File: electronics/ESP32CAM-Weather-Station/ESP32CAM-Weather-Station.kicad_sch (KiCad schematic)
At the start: 41 parts, among them IC1 BME688, IC2 SGP41-D-R4, IC3 VEML7700-TT, IC4 BQ24093DGQR, IC5 BQ29707DSET, IC6 MCP3426A0T-E_SN, IC7 TPS63070RNMR, J1 B4B-PH-SM4-TB_LF__SN_, J2 B4B-PH-SM4-TB_LF__SN_, J3 B4B-PH-SM4-TB_LF__SN_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

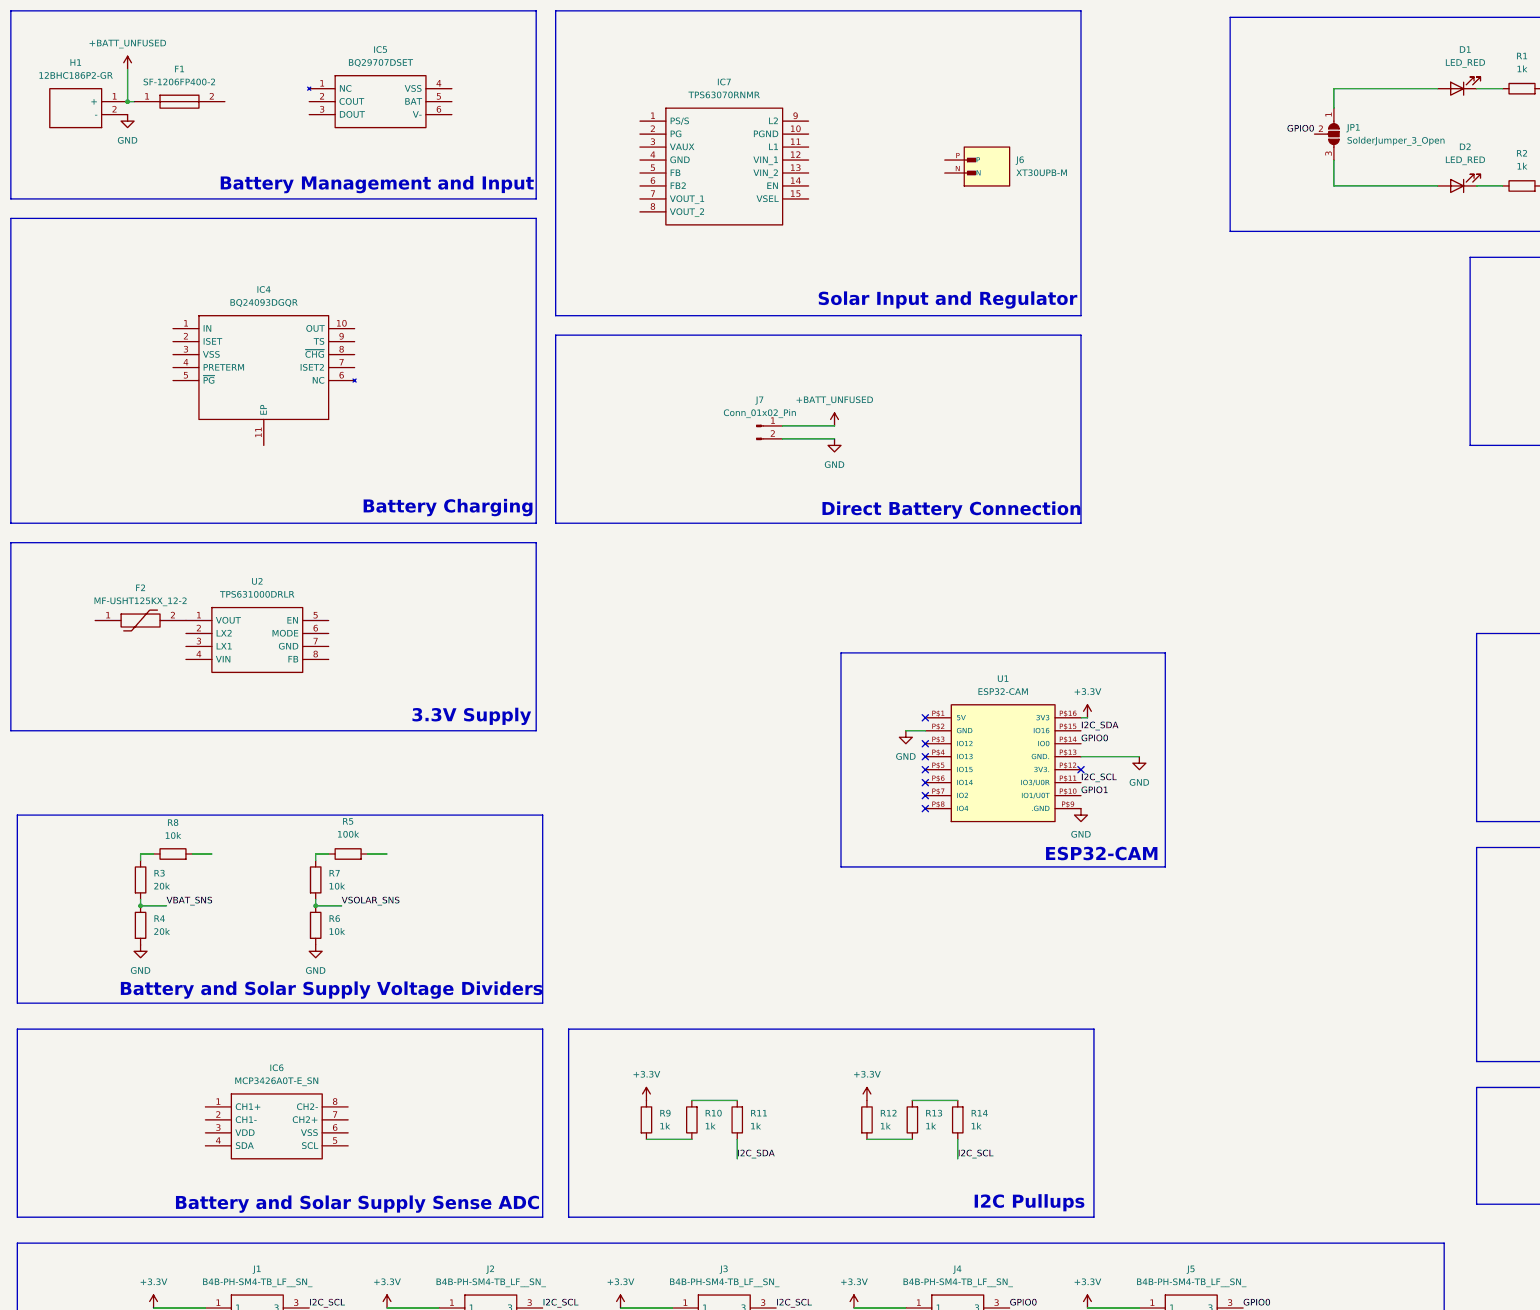
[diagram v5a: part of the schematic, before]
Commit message: [WIP] Wired battery input and protection.
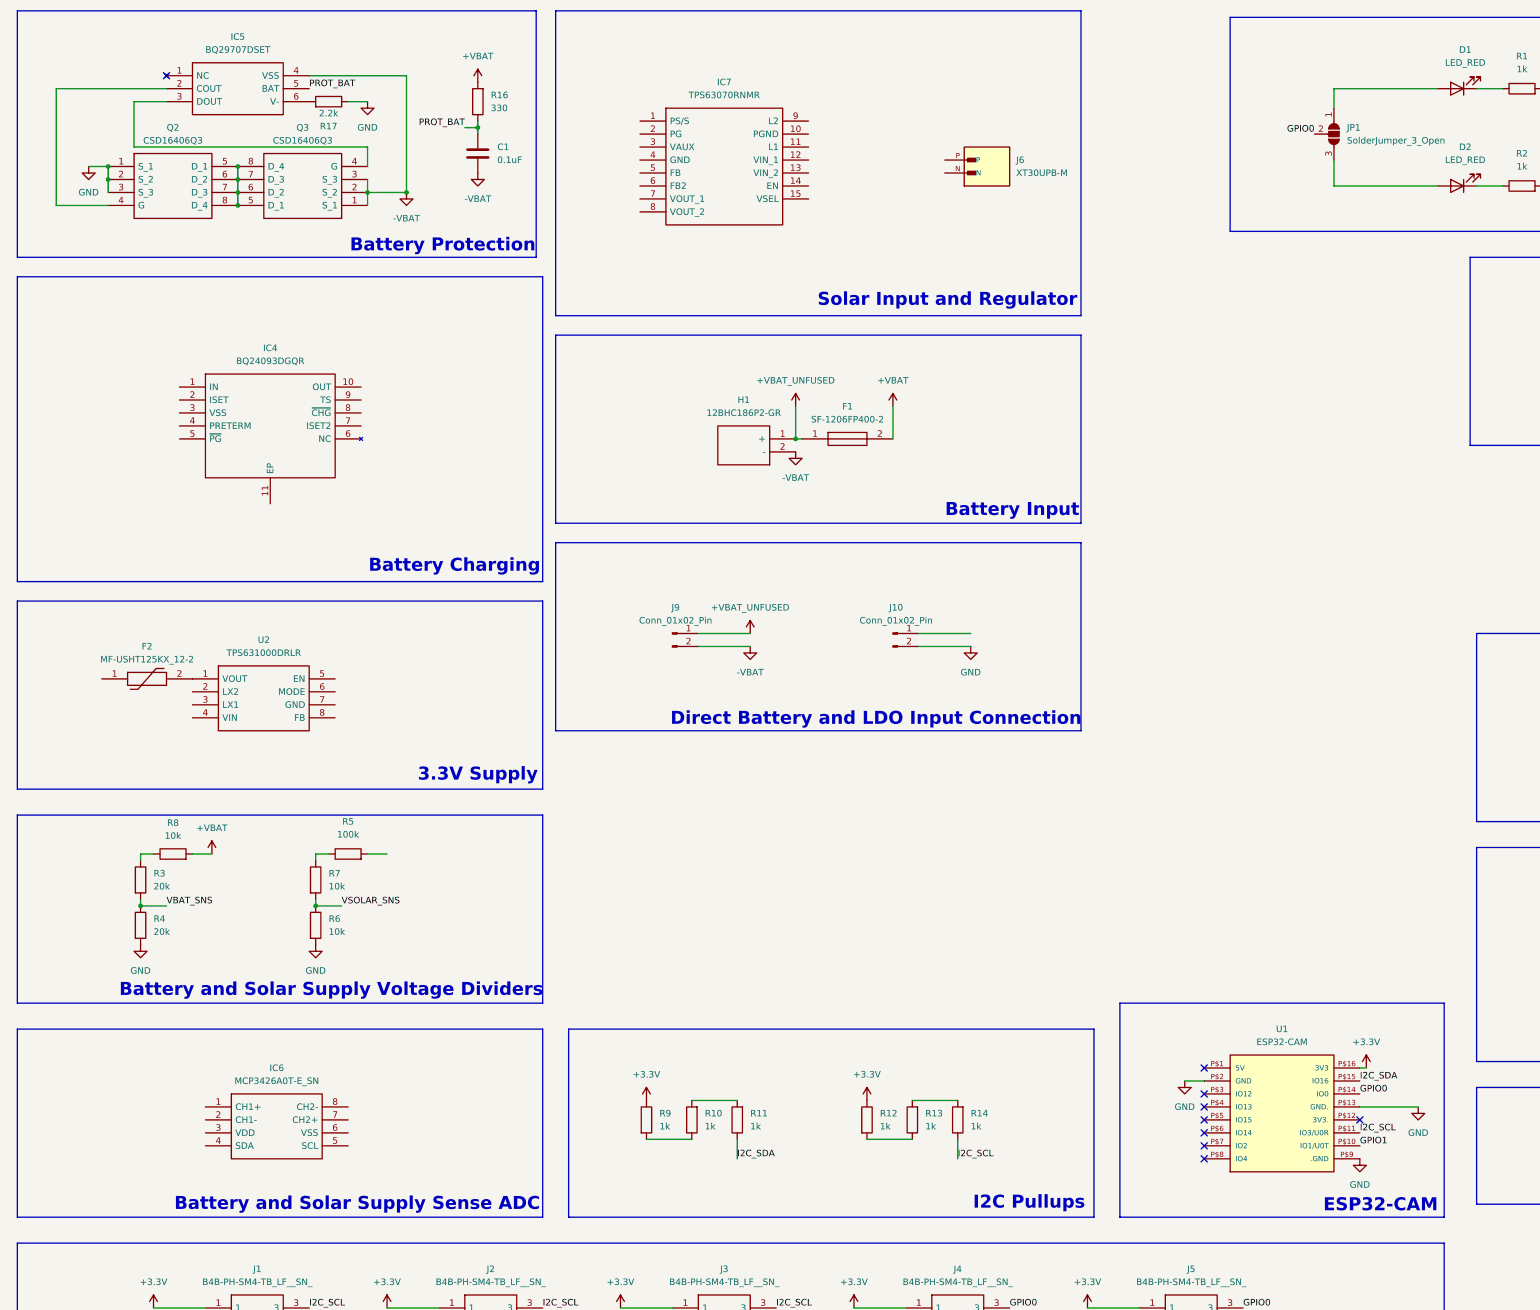
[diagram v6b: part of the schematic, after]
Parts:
- removed J7: Conn_01x02_Pin, Connector_PinHeader_2.54mm:PinHeader_1x02_P2.54mm_Vertical, symbol Connector:Conn_01x02_Pin
- added C1: 0.1uF, Capacitor_SMD:C_0805_2012Metric_Pad1.18x1.45mm_HandSolder, symbol Device:C
- added J10, J9: Conn_01x02_Pin, Connector_PinHeader_2.54mm:PinHeader_1x02_P2.54mm_Vertical, symbol Connector:Conn_01x02_Pin
- added Q2, Q3: CSD16406Q3, CSD16406Q3:DQG_VSON-CLIP, symbol CSD16406Q3:CSD16406Q3
- added R16: 330, Resistor_SMD:R_0805_2012Metric_Pad1.20x1.40mm_HandSolder, symbol Device:R
- added R17: 2.2k, Resistor_SMD:R_0805_2012Metric_Pad1.20x1.40mm_HandSolder, symbol Device:R
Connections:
- net GND: now also J10.2 (Pin_2), Q2.1 (S_1), Q2.2 (S_2), Q2.3 (S_3), R17.1; no longer H1.2 (-)
- net at IC5.2 (COUT): now also Q2.4 (G)
- net at IC5.3 (DOUT): now also Q3.4 (G)
- net -VBAT: now reaches IC5.4 (VSS)
- net -VBAT: now also H1.2 (-), C1.2, J9.2 (Pin_2), Q3.1 (S_1), Q3.2 (S_2), Q3.3 (S_3)
- net PROT_BAT: now reaches IC5.5 (BAT)
- net PROT_BAT: now also C1.1, R16.1
- net at IC5.6 (V-): now also R17.2
- net +VBAT: now reaches F1.2
- net +VBAT: now also R8.2, R16.2
- net +BATT_UNFUSED renamed +VBAT_UNFUSED
- net +VBAT_UNFUSED: now also J9.1 (Pin_1)
- new net: Q2.5 (D_1), Q2.6 (D_2), Q2.7 (D_3), Q2.8 (D_4), Q3.5 (D_1), Q3.6 (D_2), Q3.7 (D_3), Q3.8 (D_4)
- no-connect marks 10 -> 11
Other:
- note added: "Battery Input"
- note added: "Battery Protection"
- note added: "Direct Battery and LDO Input Connection"
- note removed: "Battery Management and Input"
- note removed: "Direct Battery Connection"
- moved on the sheet: F1, F2, H1, IC4, IC5, U1, U2

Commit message: [WIP] Wired battery charger for 1A charge current and 500mA preterm current.
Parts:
- removed JP2: SolderJumper_2_Open, symbol Jumper:SolderJumper_2_Open
- added C2, C3: 1uF, Capacitor_SMD:C_0805_2012Metric_Pad1.18x1.45mm_HandSolder, symbol Device:C
- added D3, D4: LED_RED, LED_SMD:LED_0805_2012Metric_Pad1.15x1.40mm_HandSolder, symbol Device:LED
- added J7: Conn_01x02_Pin, Connector_PinHeader_2.54mm:PinHeader_1x02_P2.54mm_Vertical, symbol Connector:Conn_01x02_Pin
- added JP2, JP3: SolderJumper_3_Open, symbol Jumper:SolderJumper_3_Open
- added R18, R19: 1k, Resistor_SMD:R_0805_2012Metric_Pad1.20x1.40mm_HandSolder, symbol Device:R
- added R20: 549, Resistor_SMD:R_0805_2012Metric_Pad1.20x1.40mm_HandSolder, symbol Device:R
- added R21: 10k, Resistor_SMD:R_0805_2012Metric_Pad1.20x1.40mm_HandSolder, symbol Device:R
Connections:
- net +VBAT: now also IC4.10 (OUT), C2.1, C3.1, R18.1, R19.1
- net GND: now also IC4.11 (EP), IC4.3 (VSS), IC4.7 (ISET2), C2.2, C3.2, J7.1 (Pin_1), R20.2, R21.2
- net GPIO0: now also JP1.3 (B), JP2.3 (B), JP3.3 (B); no longer JP1.2 (C)
- net GPIO1: now also JP1.1 (A), JP2.1 (A), JP3.1 (A)
- net +5V: now reaches J10.1 (Pin_1)
- net +5V: now also IC4.1 (IN)
- net at D1.2 (A): now also JP1.2 (C); no longer JP1.1 (A)
- net at R15.1: now also JP2.2 (C)
- net at D2.2 (A): now also JP3.2 (C); no longer JP1.3 (B)
- net ISET: now reaches IC4.2 (ISET)
- net ISET: now also R20.1
- net PRETERM: now reaches IC4.4 (PRETERM)
- net PRETERM: now also R21.1
- net CHG_PG: now reaches IC4.5 (~{PG})
- net CHG_PG: now also D3.1 (K)
- net CHG_CHG: now reaches IC4.8 (~{CHG})
- net CHG_CHG: now also D4.1 (K)
- net CHG_TS: now reaches IC4.9 (TS)
- net CHG_TS: now also J7.2 (Pin_2)
- new net: D3.2 (A), R18.2
- new net: D4.2 (A), R19.2
- no-connect marks 11 -> 12
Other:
- added sheet Testing Pads (testing_pads.kicad_sch)
- note added: "Thermistor Connector"
- moved on the sheet: D1, D2, IC4, JP1, LS1, Q1, R1, R15, R2, S1

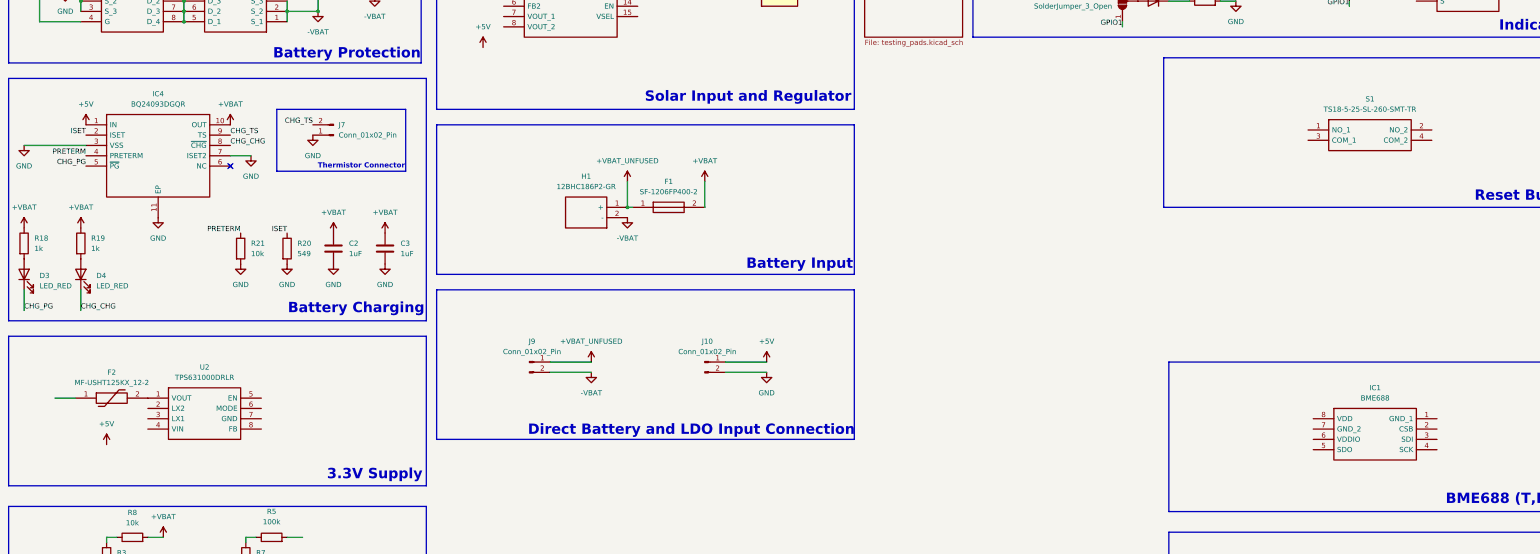
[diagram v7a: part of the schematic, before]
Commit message: [WIP] Wired 3v3 regulator.
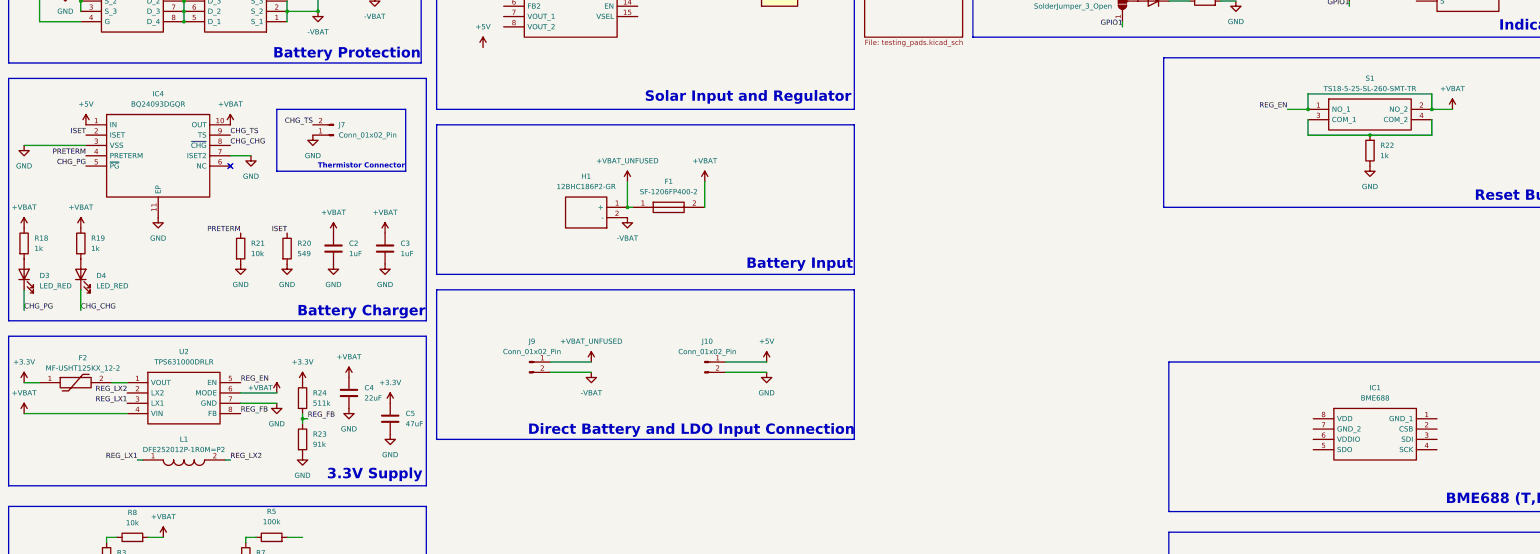
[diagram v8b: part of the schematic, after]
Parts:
- added C4: 22uF, Capacitor_SMD:C_0603_1608Metric_Pad1.08x0.95mm_HandSolder, symbol Device:C
- added C5: 47uF, Capacitor_SMD:C_0805_2012Metric_Pad1.18x1.45mm_HandSolder, symbol Device:C
- added L1: DFE252012P-1R0M=P2, DFE2HCAH1R0MJ0L, symbol DFE252012P-1R0M=P2:DFE252012P-1R0M=P2
- added R22: 1k, Resistor_SMD:R_0805_2012Metric_Pad1.20x1.40mm_HandSolder, symbol Device:R
- added R23: 91k, Resistor_SMD:R_0805_2012Metric_Pad1.20x1.40mm_HandSolder, symbol Device:R
- added R24: 511k, Resistor_SMD:R_0805_2012Metric_Pad1.20x1.40mm_HandSolder, symbol Device:R
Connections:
- net +3.3V: now also F2.1, C5.1, R24.1
- net +VBAT: now also S1.1 (NO_1), S1.2 (NO_2), U2.4 (VIN), U2.5 (EN), U2.6 (MODE), C4.1
- net GND: now also U2.7 (GND), C4.2, C5.2, R22.1, R23.2
- net REG_LX2: now reaches U2.2 (LX2)
- net REG_LX2: now also L1.2
- net REG_LX1: now reaches U2.3 (LX1)
- net REG_LX1: now also L1.1
- net REG_FB: now reaches U2.8 (FB)
- net REG_FB: now also R23.1, R24.2
- net at S1.3 (COM_1): now also S1.4 (COM_2), R22.2
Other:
- note added: "Battery Charger"
- note removed: "Battery Charging"
- moved on the sheet: F2, S1, U2
